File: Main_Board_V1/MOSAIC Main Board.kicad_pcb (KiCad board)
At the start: 2 copper layers, 89 x 89 mm, 85 parts, among them J1 CONN E, J10 QWIIC_RIGHT_ANGLE, J11 Vertical Qwiic Connector, J12 CONN E, J13 CONN E, J14 35RAPC4BH3 CONN 3.5MM, J2 CONN E, J3 CONN E, J4 CONN HEADER VERT 10POS 1.27MM, J5 USB TYPE C R/A SMT 16PIN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

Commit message: Updating JLCPCB sources
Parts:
- removed 3.3V, GND, SWDIO, VIN, V_BATT: ~, main_board_footprints_V1.0:PAD.03X.05
- added 3.3V1: ~, main_board_footprints_V1.0:PAD.03X.05, F.Cu at (194.0, 136.2)
- added GND1: ~, main_board_footprints_V1.0:PAD.03X.05, F.Cu at (192.4, 136.2)
- added SWDIO2: ~, main_board_footprints_V1.0:PAD.03X.05, F.Cu at (190.8, 136.2)
- added VIN1: ~, main_board_footprints_V1.0:PAD.03X.05, F.Cu at (189.2, 136.2)
- added V_BATT1: ~, main_board_footprints_V1.0:PAD.03X.05, F.Cu at (187.6, 136.2)
- R1: value 20k -> 19.6k

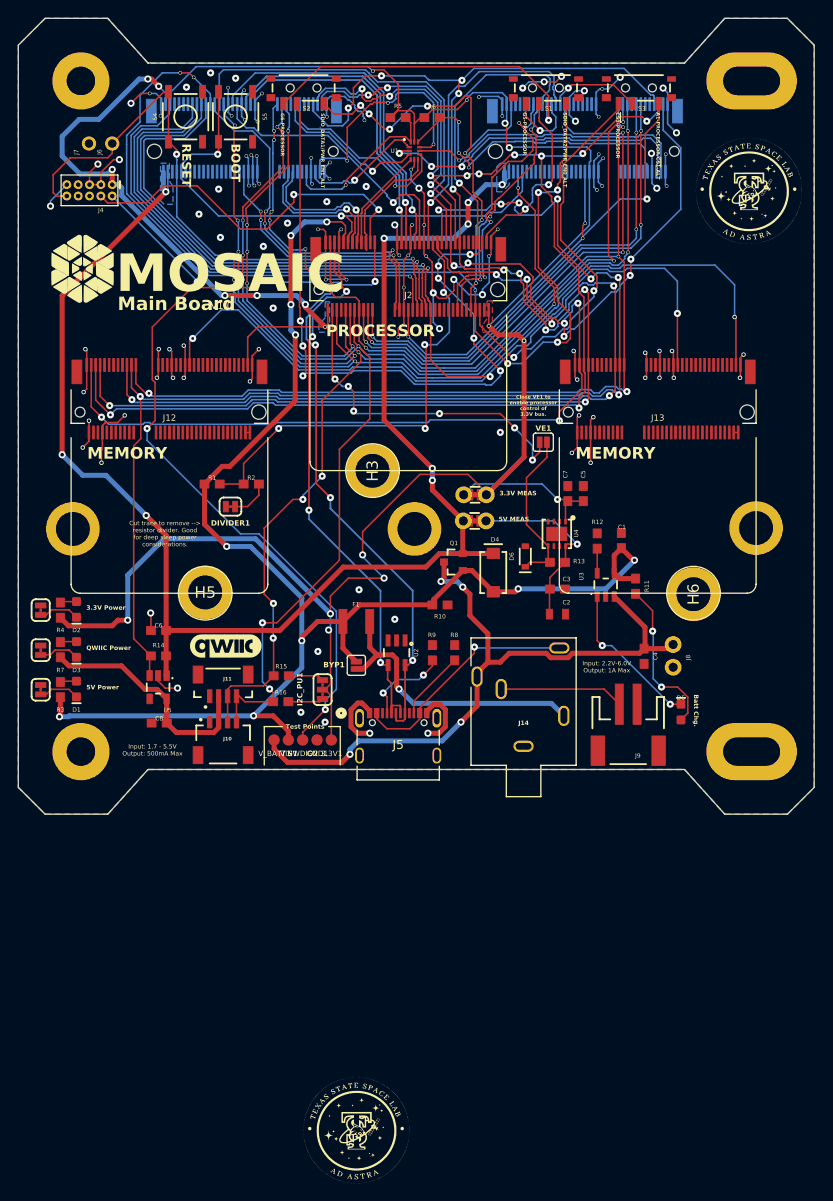
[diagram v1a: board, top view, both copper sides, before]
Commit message: Finish comp placement
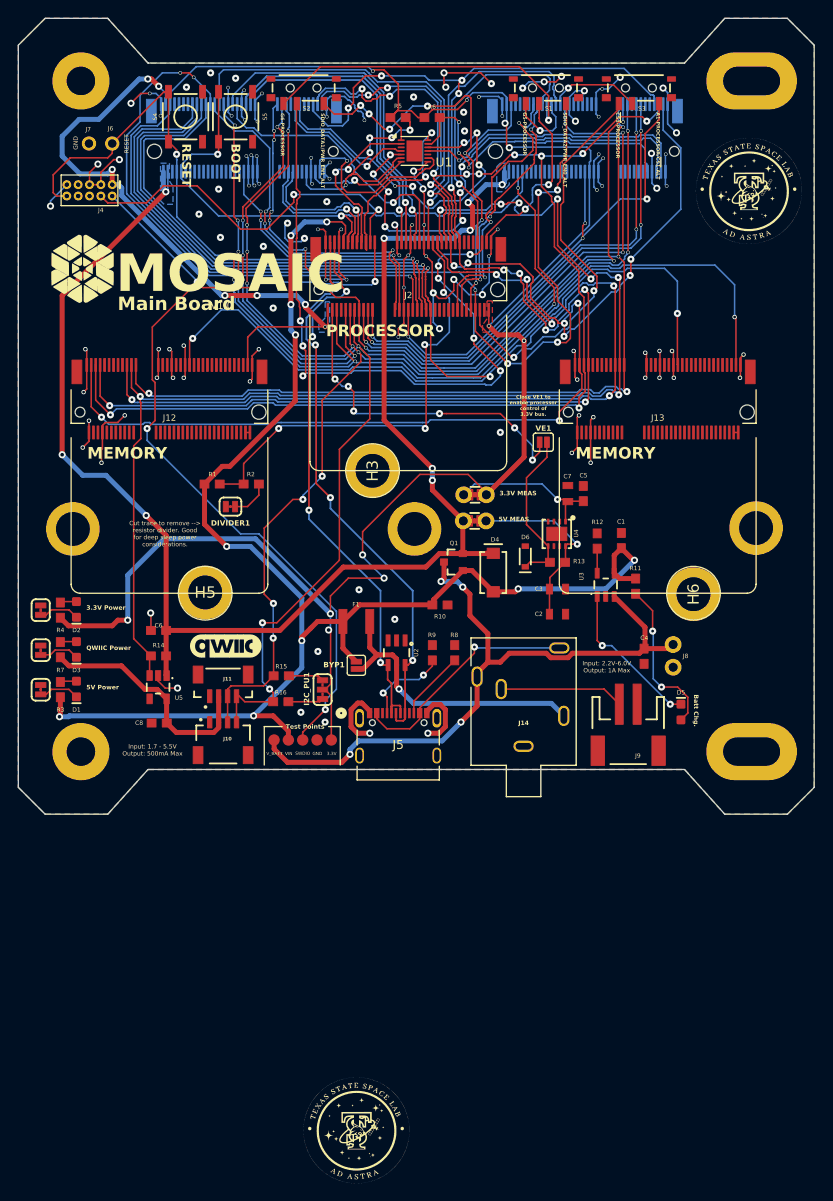
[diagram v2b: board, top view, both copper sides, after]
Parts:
- C3, C7: footprint main_board_footprints_V1.0:0603 -> main_board_footprints_V1.0:0805
- J10: value QWIIC_RIGHT_ANGLE -> Right Angle Qwiic Connector
- U1: value IC SWITCH SP3T X 2 1OHM 12QFN -> IC SWITCH SP3T X 2 750mOhm TDFN-14(3x3); footprint main_board_footprints_V1.0:STG3856 -> main_board_footprints_V1.0:TDFN-14-1EP_3x3mm_P0.4mm_EP1.78x2.35mm
- renumbered 3.3V1 to 3.3V, GND1 to GND, SWDIO2 to SWDIO, VIN1 to VIN, V_BATT1 to V_BATT
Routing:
- net /RX1-PROCESSOR-PLEX: track 21.9 -> 40.2 mm, vias 1 -> 5
- net /TX1-DFU_RX-FC1-PLEX: track 36.0 -> 54.1 mm, vias 3 -> 7
- net GND: track 236.8 -> 249.0 mm, vias 113 -> 119
- net /~{DFU-FC0}: track 19.2 -> 26.5 mm, vias 1 -> 5
- net /TX1-PROCESSOR: track 11.5 -> 18.3 mm, vias 0 -> 2
- net /RX1-PROCESSOR: track 14.4 -> 20.6 mm, vias 0 -> 2
- net /RX1-DFU_TX-FC0-PLEX: track 26.7 -> 20.8 mm, vias 3 -> 1
- net /TX1-DFU_RX-FC0-PLEX: track 14.0 -> 12.1 mm
- net /TX1-PROCESSOR-PLEX: track 17.8 -> 16.6 mm
- net /~{BOOT}: track 60.3 -> 61.4 mm
- net VCC: track 169.5 -> 170.4 mm
- net /RX1-DFU_TX-FC1-PLEX: track 32.7 -> 31.7 mm
- net /~{CS0}-PROCESSOR: track 47.4 -> 48.2 mm
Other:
- board text added: "GND"

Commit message: Finished JLCPCB setup
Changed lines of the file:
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@@
 			)
 		)
+		(property "FT Rotation Offset" "180"
+			(at 0 0 270)
+			(unlocked yes)
+			(layer "F.Fab")
+			(hide yes)
+			(effects
+				(font
+					(size 1 1)
+					(thickness 0.15)
+				)
+			)
+		)
 		(sheetname "/")
 		(sheetfile "MOSAIC Main Board.kicad_sch")
@@
 			)
 		)
+		(property "FT Rotation Offset" "180"
+			(at 0 0 90)
+			(unlocked yes)
+			(layer "F.Fab")
+			(hide yes)
+			(effects
+				(font
+					(size 1 1)
+					(thickness 0.15)
+				)
+			)
+		)
 		(sheetname "/")
 		(sheetfile "MOSAIC Main Board.kicad_sch")
@@
 			)
 		)
+		(property "FT Rotation Offset" "180"
+			(at 0 0 90)
+			(unlocked yes)
+			(layer "F.Fab")
+			(hide yes)
+			(effects
+				(font
+					(size 1 1)
+					(thickness 0.15)
+				)
+			)
+		)
 		(sheetname "/")
 		(sheetfile "MOSAIC Main Board.kicad_sch")
@@
 			)
 		)
+		(property "FT Rotation Offset" "-90"
+			(at 0 0 90)
+			(unlocked yes)
+			(layer "F.Fab")
+			(hide yes)
+			(effects
+				(font
+					(size 1 1)
+					(thickness 0.15)
+				)
+			)
+		)
 		(sheetname "/")
 		(sheetfile "MOSAIC Main Board.kicad_sch")
@@
 			)
 		)
+		(property "FT Rotation Offset" "180"
+			(at 0 0 0)
+			(unlocked yes)
+			(layer "F.Fab")
+			(hide yes)
+			(effects
+				(font
+					(size 1 1)
+					(thickness 0.15)
+				)
+			)
+		)
 		(sheetname "/")
 		(sheetfile "MOSAIC Main Board.kicad_sch")
@@
 			)
 		)
+		(property "FT Rotation Offset" "180"
+			(at 0 0 270)
+			(unlocked yes)
+			(layer "F.Fab")
+			(hide yes)
+			(effects
+				(font
+					(size 1 1)
+					(thickness 0.15)
+				)
+			)
+		)
 		(sheetname "/")
 		(sheetfile "MOSAIC Main Board.kicad_sch")
@@
 			)
 		)
-		(property "Datasheet" "https://www.digikey.com/en/products/detail/kemet/C0603C104J4RAC7867/411096"
+		(property "Datasheet" "https://jlcpcb.com/api/file/downloadByFileSystemAccessId/8590922676573577216"
 			(at 0 0 0)
 			(layer "F.Fab")
@@
 			)
 		)
-		(property "Description" "https://jlcpcb.com/partdetail/-KAF21BR71H104JT/C18212337"
+		(property "Description" "https://jlcpcb.com/partdetail/21992639-0805CG0R1C500NT/C20617880"
 			(at 0 0 0)
 			(layer "F.Fab")
@@
 			)
 		)
-		(property "JLCPCB Part #" "C18212337"
+		(property "JLCPCB Part #" "C20617880"
 			(at 0 0 0)
 			(unlocked yes)
@@
 			)
 		)
+		(property "FT Rotation Offset" "180"
+			(at 0 0 180)
+			(unlocked yes)
+			(layer "F.Fab")
+			(hide yes)
+			(effects
+				(font
+					(size 1 1)
+					(thickness 0.15)
+				)
+			)
+		)
 		(sheetname "/")
 		(sheetfile "MOSAIC Main Board.kicad_sch")
@@
 			)
 		)
+		(property "FT Rotation Offset" "180"
+			(at 0 0 0)
+			(unlocked yes)
+			(layer "F.Fab")
+			(hide yes)
+			(effects
+				(font
+					(size 1 1)
+					(thickness 0.15)
+				)
+			)
+		)
 		(sheetname "/")
 		(sheetfile "MOSAIC Main Board.kicad_sch")
@@
 			)
 		)
+		(property "FT Rotation Offset" "180"
+			(at 0 0 0)
+			(unlocked yes)
+			(layer "F.Fab")
+			(hide yes)
+			(effects
+				(font
+					(size 1 1)
+					(thickness 0.15)
+				)
+			)
+		)
 		(sheetname "/")
 		(sheetfile "MOSAIC Main Board.kicad_sch")
@@
 			)
 		)
+		(property "FT Rotation Offset" "180"
+			(at 0 0 270)
+			(unlocked yes)
+			(layer "F.Fab")
+			(hide yes)
+			(effects
+				(font
+					(size 1 1)
+					(thickness 0.15)
+				)
+			)
+		)
 		(sheetname "/")
 		(sheetfile "MOSAIC Main Board.kicad_sch")
@@
 		(descr "<h3>SMD- 4 Pin Right Angle </h3>\n<p>Specifications:\n<ul><li>Pin count:4</li>\n<li>Pin pitch:0.1\"</li>\n</ul></p>\n<p>Example device(s):\n<ul><li>CONN_04</li>\n</ul></p>")
 		(property "Reference" "J10"
-			(at 0 2.075 0)
+			(at -1.397 2.159 0)
 			(layer "F.SilkS")
 			(effects
 				(font
-					(size 0.4 0.4)
-					(thickness 0.1)
-					(bold yes)
+					(size 0.48768 0.48768)
+					(thickness 0.12192)
 				)
 				(justify left bottom)
@@
 			)
 		)
-		(property "Datasheet" "https://jlcpcb.com/api/file/downloadByFileSystemAccessId/8588895674171052032"
+		(property "Datasheet" "https://jlcpcb.com/api/file/downloadByFileSystemAccessId/8590907288981364736"
 			(at 0 0 0)
 			(layer "F.Fab")
@@
 			)
 		)
-		(property "Description" "https://jlcpcb.com/partdetail/C145956"
+		(property "Description" "https://jlcpcb.com/partdetail/Lian_XinTechnology-XDWF_091004P/C7527619"
 			(at 0 0 0)
 			(layer "F.Fab")
@@
 			)
 		)
-		(property "JLCPCB Part #" "C145956"
+		(property "JLCPCB Part #" "C7527619"
 			(at 0 0 0)
 			(unlocked yes)
@@
 			)
 		)
+		(property "FT Rotation Offset" "-90"
+			(at 0 0 0)
+			(unlocked yes)
+			(layer "F.Fab")
+			(hide yes)
+			(effects
+				(font
+					(size 1 1)
+					(thickness 0.15)
+				)
+			)
+		)
 		(sheetname "/")
 		(sheetfile "MOSAIC Main Board.kicad_sch")
@@
 			(at 0 0 180)
 			(unlocked yes)
+			(layer "F.Fab")
+			(hide yes)
+			(effects
+				(font
+					(size 1 1)
+					(thickness 0.15)
+				)
+			)
+		)
+		(property "FT Rotation Offset" "-90"
+			(at 0 0 180)
+			(unlocked yes)

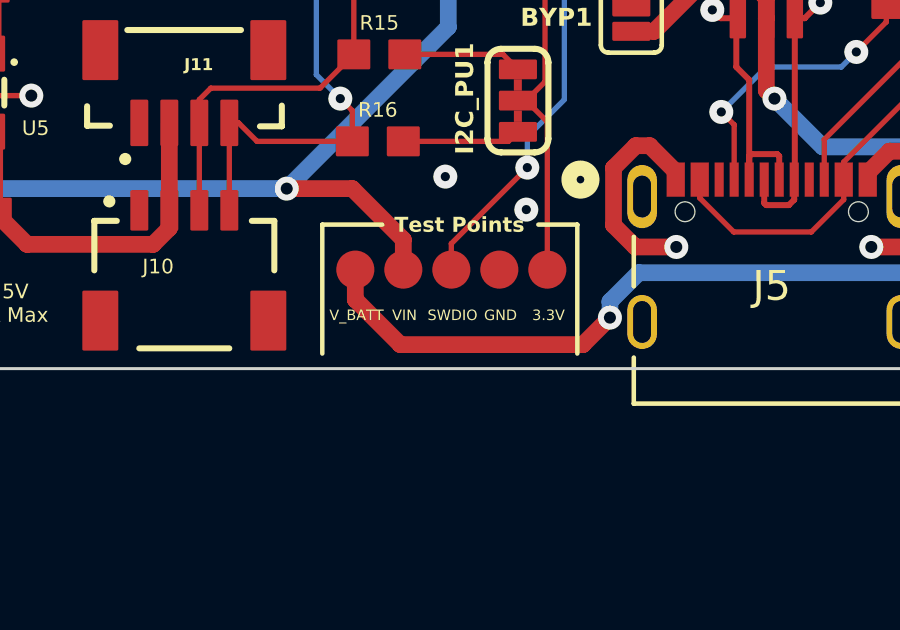
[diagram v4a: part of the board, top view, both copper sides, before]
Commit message: added bom
Added bom for assembly after JLCPCB assembly.
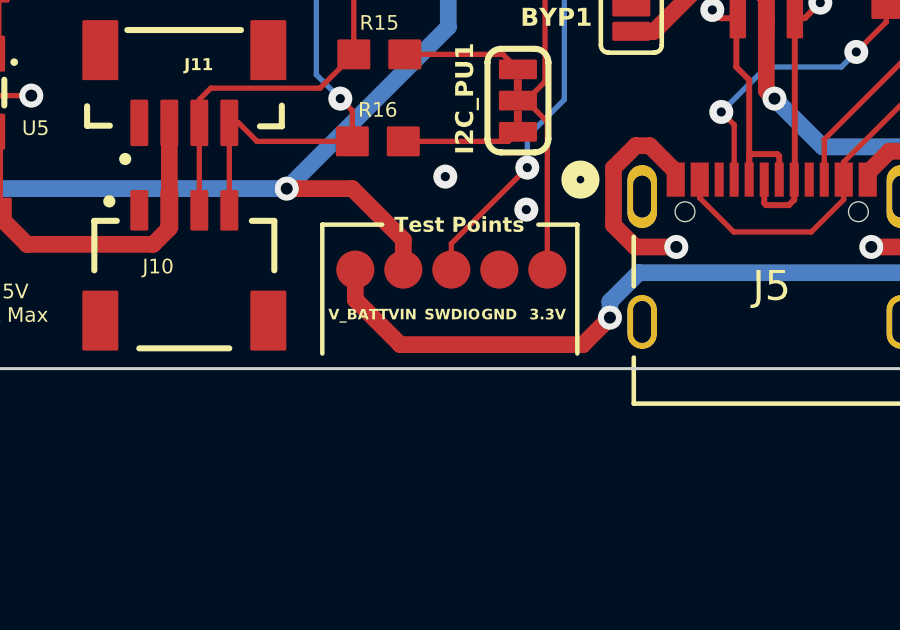
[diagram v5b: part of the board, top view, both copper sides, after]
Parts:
- removed 3.3V, GND, SWDIO, VIN, V_BATT: ~, main_board_footprints_V1.0:PAD.03X.05
- added 3.3V1: ~, main_board_footprints_V1.0:PAD.03X.05, F.Cu at (194.0, 136.2)
- added GND1: ~, main_board_footprints_V1.0:PAD.03X.05, F.Cu at (192.4, 136.2)
- added SWDIO1: ~, main_board_footprints_V1.0:PAD.03X.05, F.Cu at (190.8, 136.2)
- added VIN1: ~, main_board_footprints_V1.0:PAD.03X.05, F.Cu at (189.2, 136.2)
- added V_BATT1: ~, main_board_footprints_V1.0:PAD.03X.05, F.Cu at (187.6, 136.2)
- J9: value BATT JST-2-SMD -> CONN_JST_BATT
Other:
- board text added: "3.3V"
- board text added: "SWDIO"
- board text added: "VIN"
- board text added: "V_BATT"
